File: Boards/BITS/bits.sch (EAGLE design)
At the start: 38 parts, among them T1 SI1013, U1 LMR16020, X1 22-23-2021, X2 53398-10, X3 22-23-2031, X4 22-23-2041

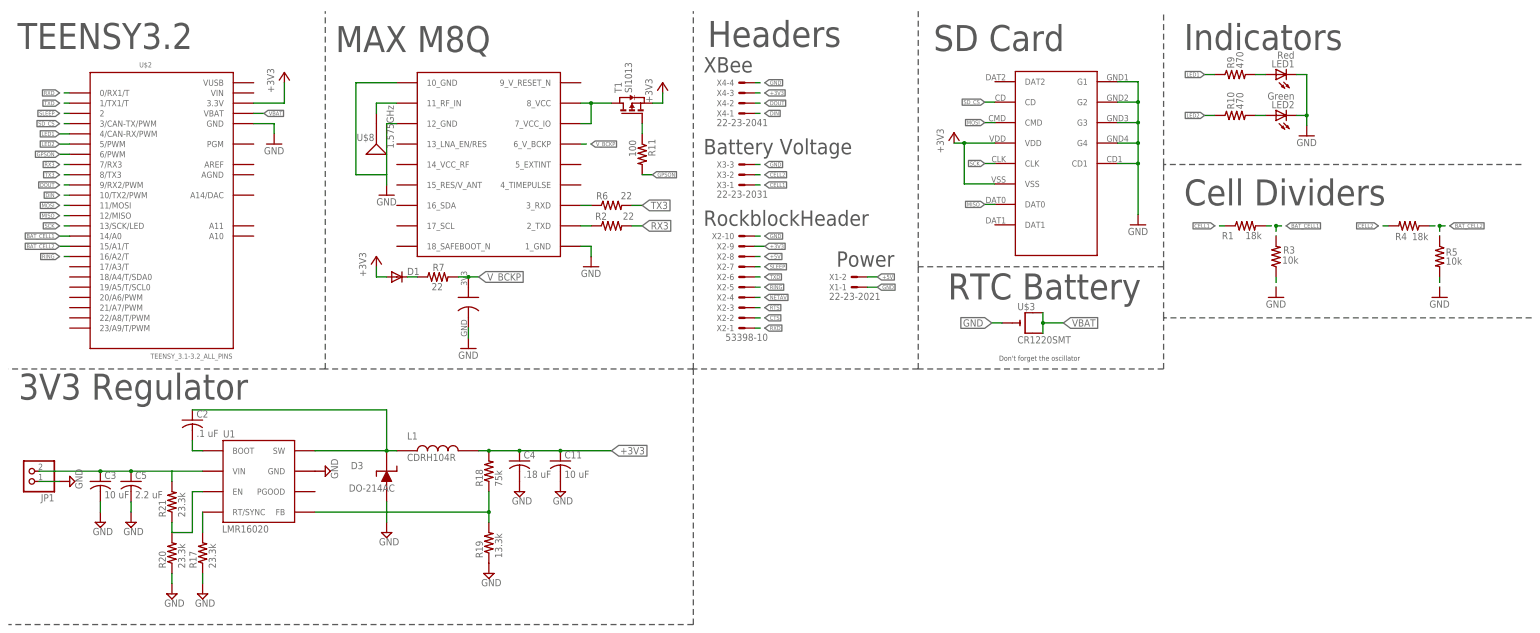
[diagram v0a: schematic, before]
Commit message: Integrate the BITS XBee
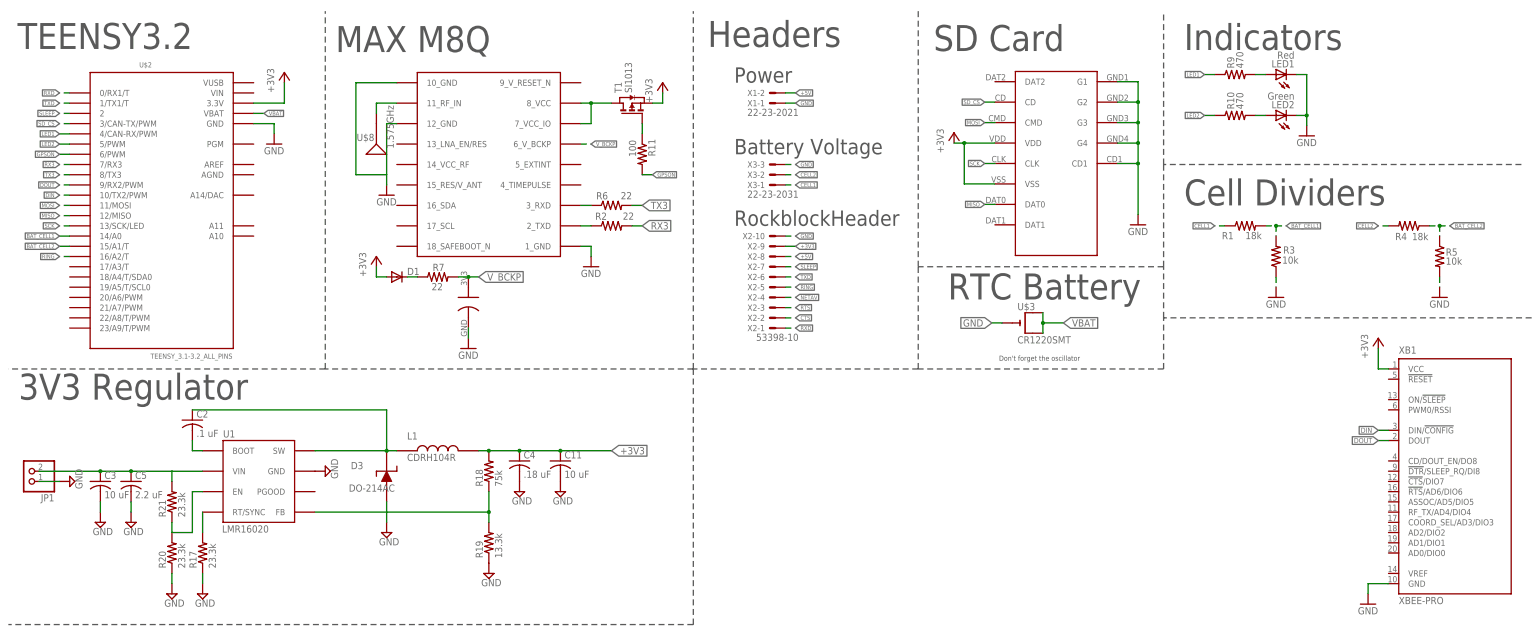
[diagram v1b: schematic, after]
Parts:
- removed X4: 22-23-2041, con-molex:22-23-2041
- added XB1: XBEE-PRO, maxstream:XBEE-PRO
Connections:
- net +3V3: now also XB1.VCC; no longer X4-3.S
- net DIN: now also XB1.DIN/!CONFIG; no longer X4-1.S
- net DOUT: now also XB1.DOUT; no longer X4-2.S
- net GND: now also XB1.GND; no longer X4-4.S
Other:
- note removed: "XBee"
- moved on the sheet: X1-1, X1-2, X2-1, X2-10, X2-2, X2-3, X2-4, X2-5, X2-6, X2-7, X2-8, X2-9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
